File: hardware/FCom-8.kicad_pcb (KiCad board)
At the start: 12 copper layers, 94 x 127 mm, 85 parts, among them J101 Conn_01x04, J201 4090 USB-C, J202 9V battery, SW101 SW_DIP_x08, SW102 SW_DIP_x08, SW104 SW_DIP_x04, SW105 G19AP, SW301 Q/1/STOP, SW302 W/2/CH0, SW303 E/3/CH1, SW304 R/4/CH2, SW305 T/5/CH3, SW306 Y/6/_, SW307 U/7/-, SW308 I/8/+, SW309 O/9/=, SW310 P/0, SW311 A/!/`, SW312 S/"/CH4, SW313 D/$/CH5, SW314 F/%/CH6, SW315 G/^/CH7, SW316 H/&/{, SW317 J/*/}, SW318 K/(/[, SW319 L/)/], SW320 BKSP/DEL, SW321 SHIFT, SW322 Z/\/|, SW323 X/;/:, SW324 C/'/@, SW325 V/#/~, SW326 B/,/<, SW327 N/./>, SW328 M///?, SW329 SYM, SW330 SPC/ENT, U101 W65C02S6TPG-14, U102 AS6C1008-55PCN, U103 W65C22N6TPG-14, U104 74LS04, U105 74LS08, U106 74LS21, U201 LP2954AIT/NOPB, U301 MCP23S17_SP, U302 NHD-0420DZ-NSW-BBW, Y101 ECS-100AX-010

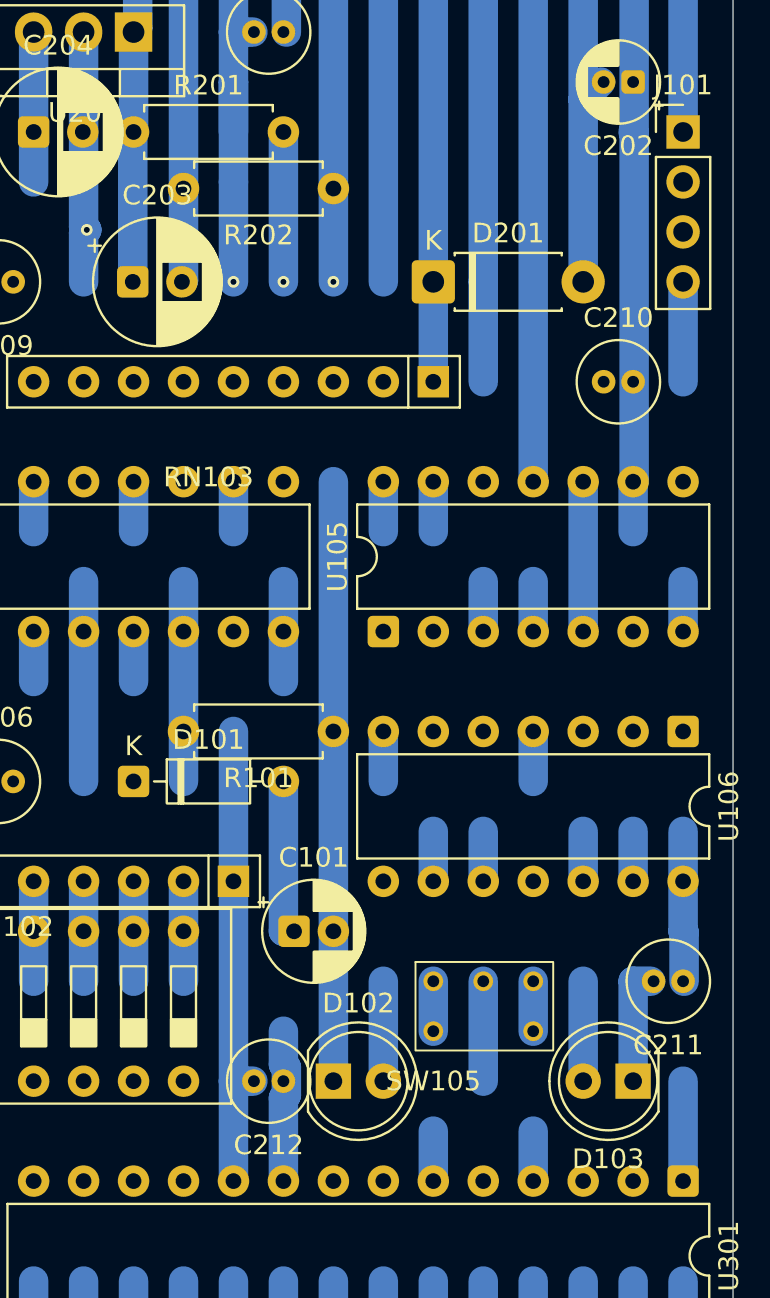
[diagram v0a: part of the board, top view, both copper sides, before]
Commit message: Swap direction of CPU run/RAM write switch for ergonomics
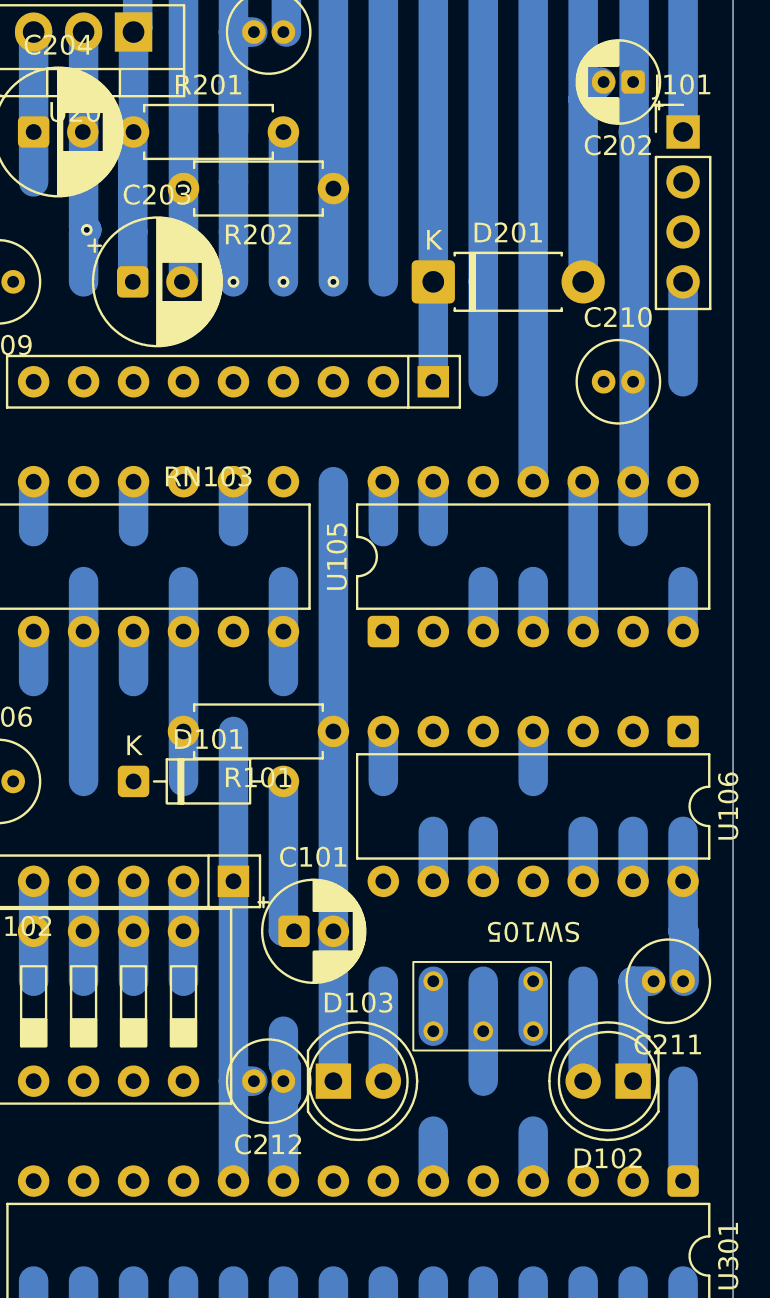
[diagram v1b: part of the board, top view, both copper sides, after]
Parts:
- moved D102 15.2 mm to (139.7, 104.1), turned to 180 degrees
- moved D103 15.2 mm to (124.5, 104.1), turned to 0 degrees
- moved SW105 5.68 mm to (134.6, 101.6), turned to 180 degrees
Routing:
- net Net-(D103-A): track 44.4 -> 30.5 mm
- net +5V: track 186.4 -> 195.3 mm
- net VCC: track 527.6 -> 535.9 mm
- net GND: track 786.3 -> 792.6 mm
- net Net-(D102-A): track 58.6 -> 53.8 mm
- net VBS: track 190.5 -> 192.0 mm
